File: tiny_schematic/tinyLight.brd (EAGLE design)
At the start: 52 x 33.2 mm, 37 parts, among them IC1 NCP1117, IC2 XMEGA-A4TQFP, IC3 CM1293A-02SR, J1 RASM722PX, J2 Molex, J3 PDI, Q1 BC849SMD, Q2 BC849SMD, X1 MICRO-USB

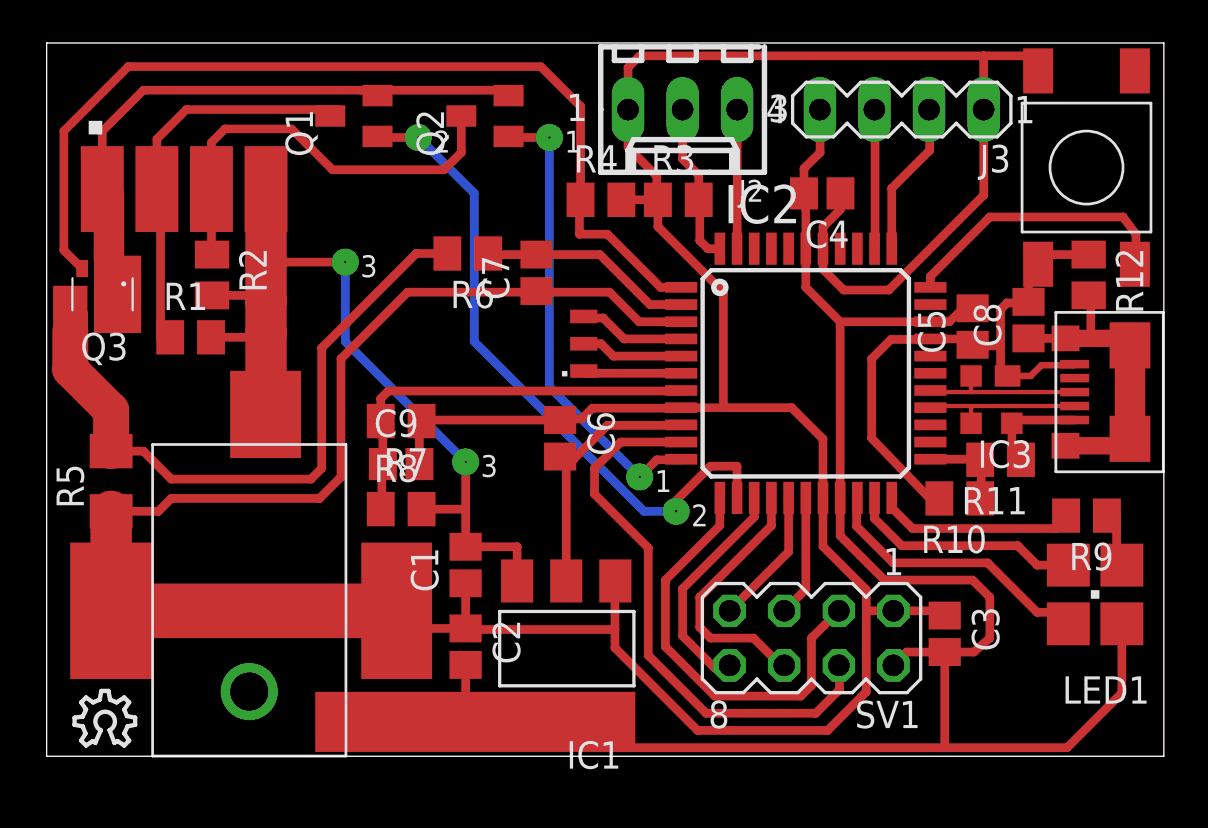
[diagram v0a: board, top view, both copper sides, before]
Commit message: Added Uart and Ir-Header
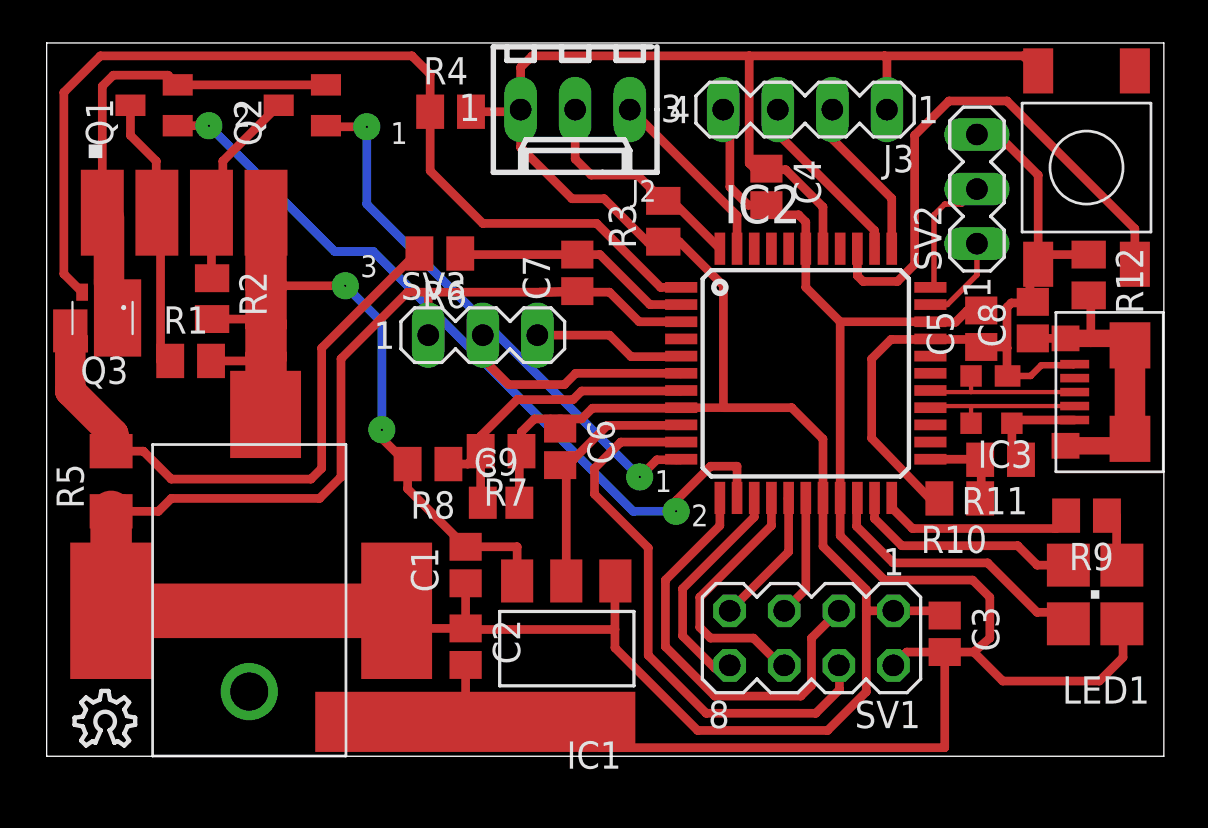
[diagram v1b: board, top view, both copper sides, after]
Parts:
- removed JP2: SMD_3PIN, tinyLight:SMD_PIN3
- added SV2, SV3: (no value), con-lstb:MA03-1
- moved Q1 9.31 mm to (5.00, 30.3)
- moved Q2 8.51 mm to (11.9, 30.3)
- moved R4 8.11 mm to (18.8, 30.0)
- moved J2 5.00 mm to (24.6, 30.1)
- moved C9 4.99 mm to (21.1, 11.8)
- moved R7 4.86 mm to (21.1, 14.2)
- moved J3 4.50 mm to (35.3, 30.1)
- moved C4 2.62 mm to (33.5, 26.5), turned to 270 degrees
- moved R8 2.44 mm to (17.8, 13.6), turned to 180 degrees
- moved C7 1.90 mm to (24.7, 22.5)
- moved R6 1.30 mm to (18.3, 23.4)
- moved R3 1.22 mm to (28.7, 24.9), turned to 90 degrees
- moved Q3 1.10 mm to (2.60, 20.4)
- moved R1 1.10 mm to (6.70, 18.4)
- moved JP1 1.10 mm to (6.40, 25.3)
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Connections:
- removed net N$1: IC2.4, JP2.3
- removed net PB: IC2.33, S1.1, S1.2
- new net N$10: IC2.33, SV2.2
- new net N$11: IC2.32, SV2.1
- new net N$12: IC2.36, S1.1, S1.2
- net GND: now also SV2.3, SV3.1
- net N$2: now also SV3.2; no longer JP2.1
- net N$27: now also SV3.3; no longer JP2.2
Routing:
- net N$12: track 0.00 -> 25.5 mm
- net PB: track 13.1 -> 0.00 mm
- net GND: track 210.3 -> 221.8 mm
- net CK: track 20.2 -> 9.60 mm
- net VGND: track 37.6 -> 29.1 mm
- net N$2: track 4.61 -> 11.1 mm
- net DATA: track 19.6 -> 13.4 mm
- net GND_IO: track 31.3 -> 25.1 mm
- net N$10: track 0.00 -> 6.04 mm
- net LED_DATA: track 30.6 -> 36.1 mm
- net N$1: track 4.98 -> 0.00 mm
- net U_PSU: track 19.8 -> 15.1 mm
- net +5V: track 41.6 -> 37.3 mm
- net N$11: track 0.00 -> 4.20 mm
- net LED_CLK: track 21.7 -> 25.8 mm
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
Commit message: Improved clearance, fixed ground routing
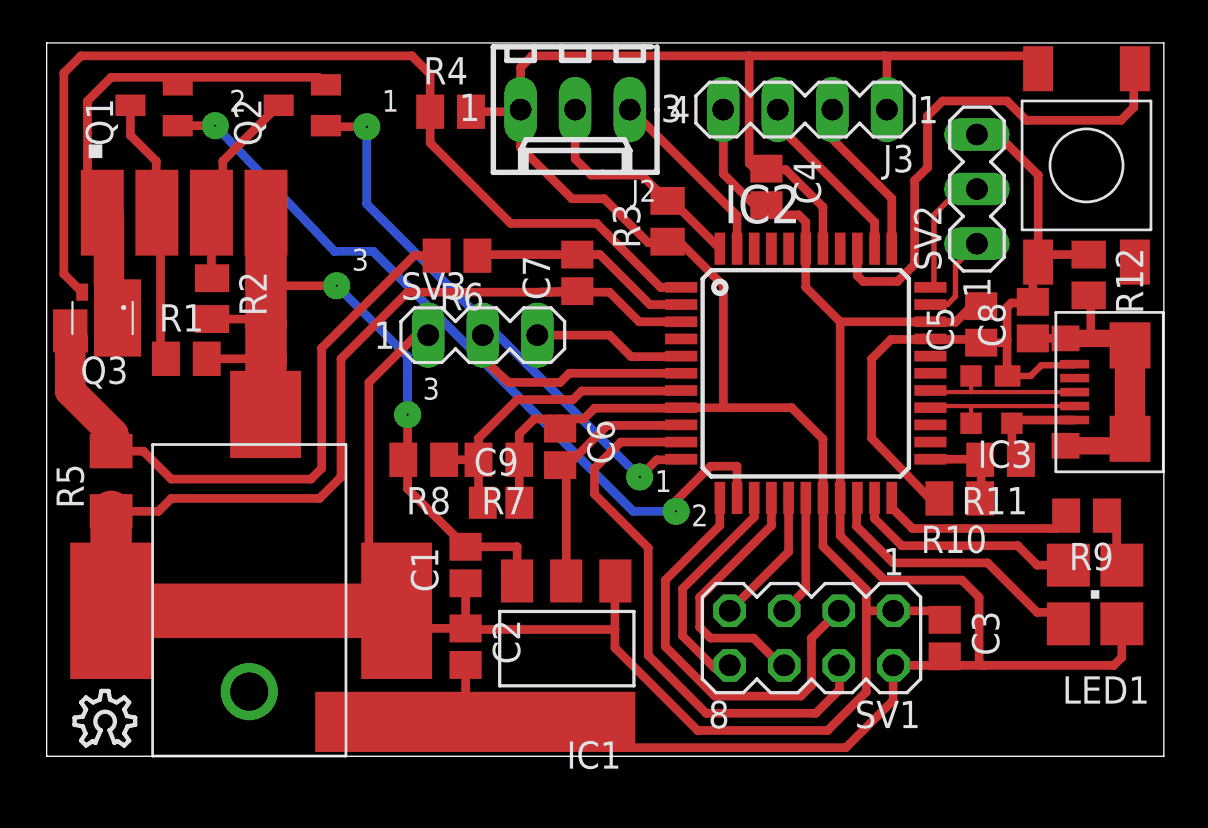
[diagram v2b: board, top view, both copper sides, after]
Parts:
- moved R6 0.81 mm to (19.1, 23.3)
- moved R7 0.41 mm to (21.1, 13.8)
- moved R8 0.28 mm to (17.6, 13.8)
- moved R1 0.22 mm to (6.50, 18.5)
- moved C5 0.20 mm to (43.5, 20.1)
- moved C3 0.20 mm to (41.8, 5.50)
- moved R3 0.20 mm to (28.9, 24.9)
- moved S1 0.10 mm to (48.4, 27.5)
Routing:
- net GND: track 221.8 -> 234.2 mm
- net +3V3: track 97.4 -> 92.6 mm
- net N$12: track 25.5 -> 24.0 mm
- net I_LED: track 11.4 -> 10.5 mm
- net GND_IO: track 25.1 -> 26.0 mm
- net VGND: track 29.1 -> 29.8 mm
